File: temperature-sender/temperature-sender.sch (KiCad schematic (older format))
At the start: 33 parts, among them K1 SERVO, P1 CONN_01X02, P2 CONN_01X02, P3 CONN_01X02, P4 CONN_01X02, P5 CONN_01X02, P6 MICRO-USB-RCT, P7 CONN_01X01, P8 CONN_01X05, SW1 SW_PUSH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

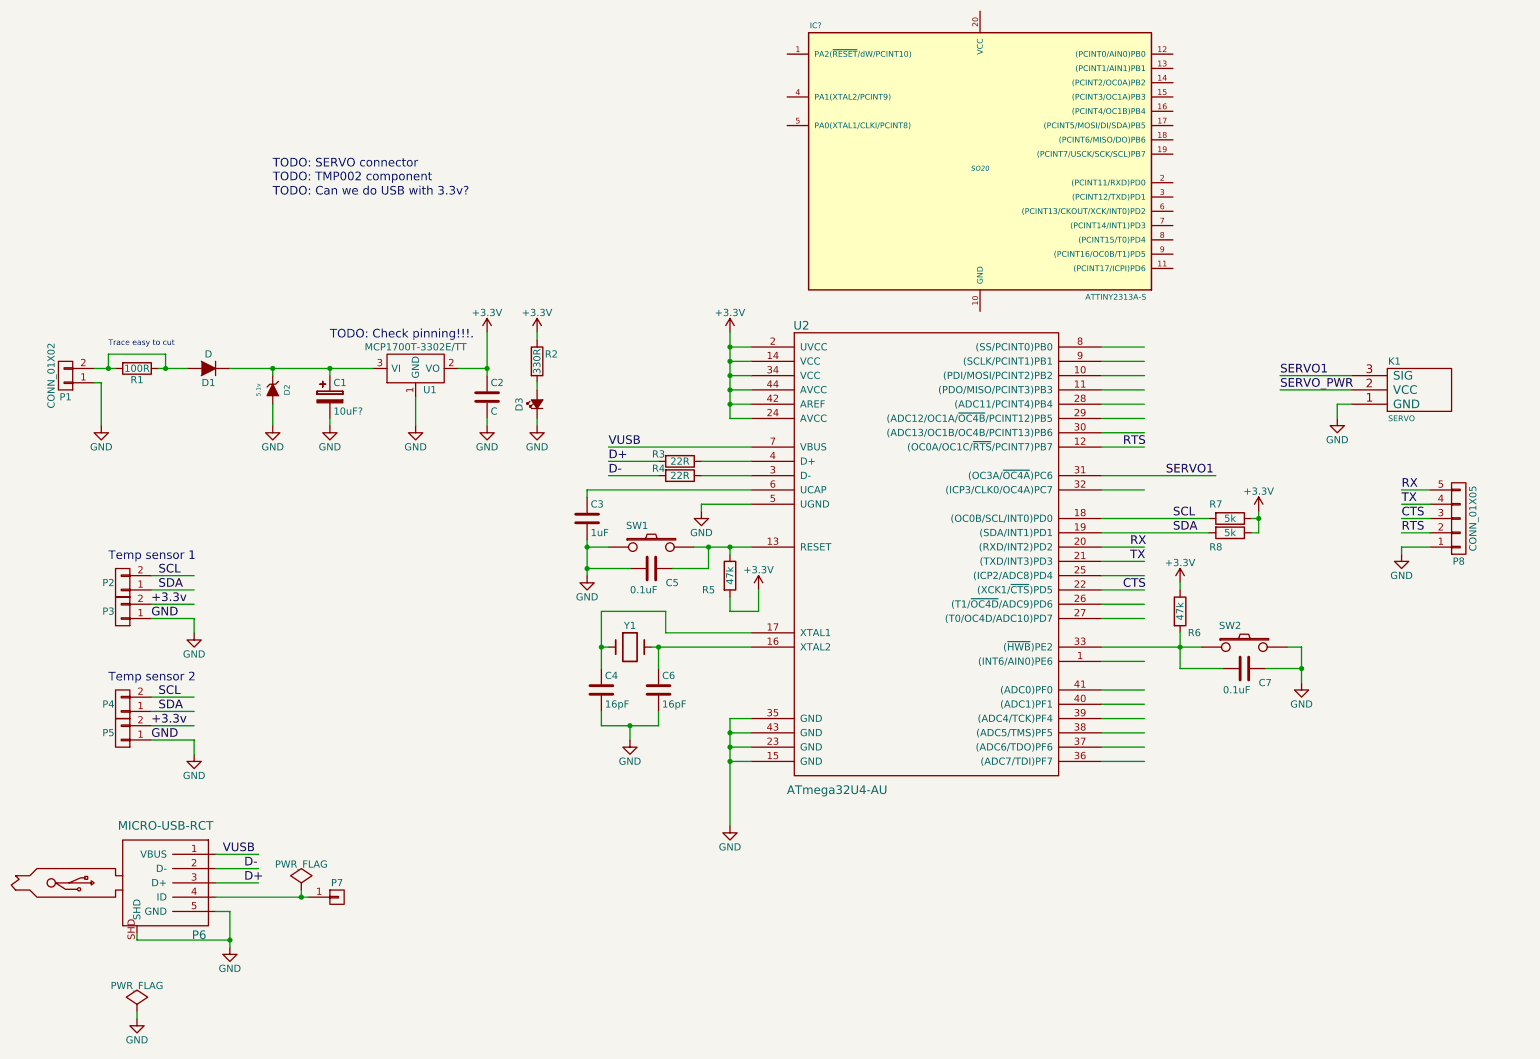
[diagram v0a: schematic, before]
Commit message: More changes to temperature-sender
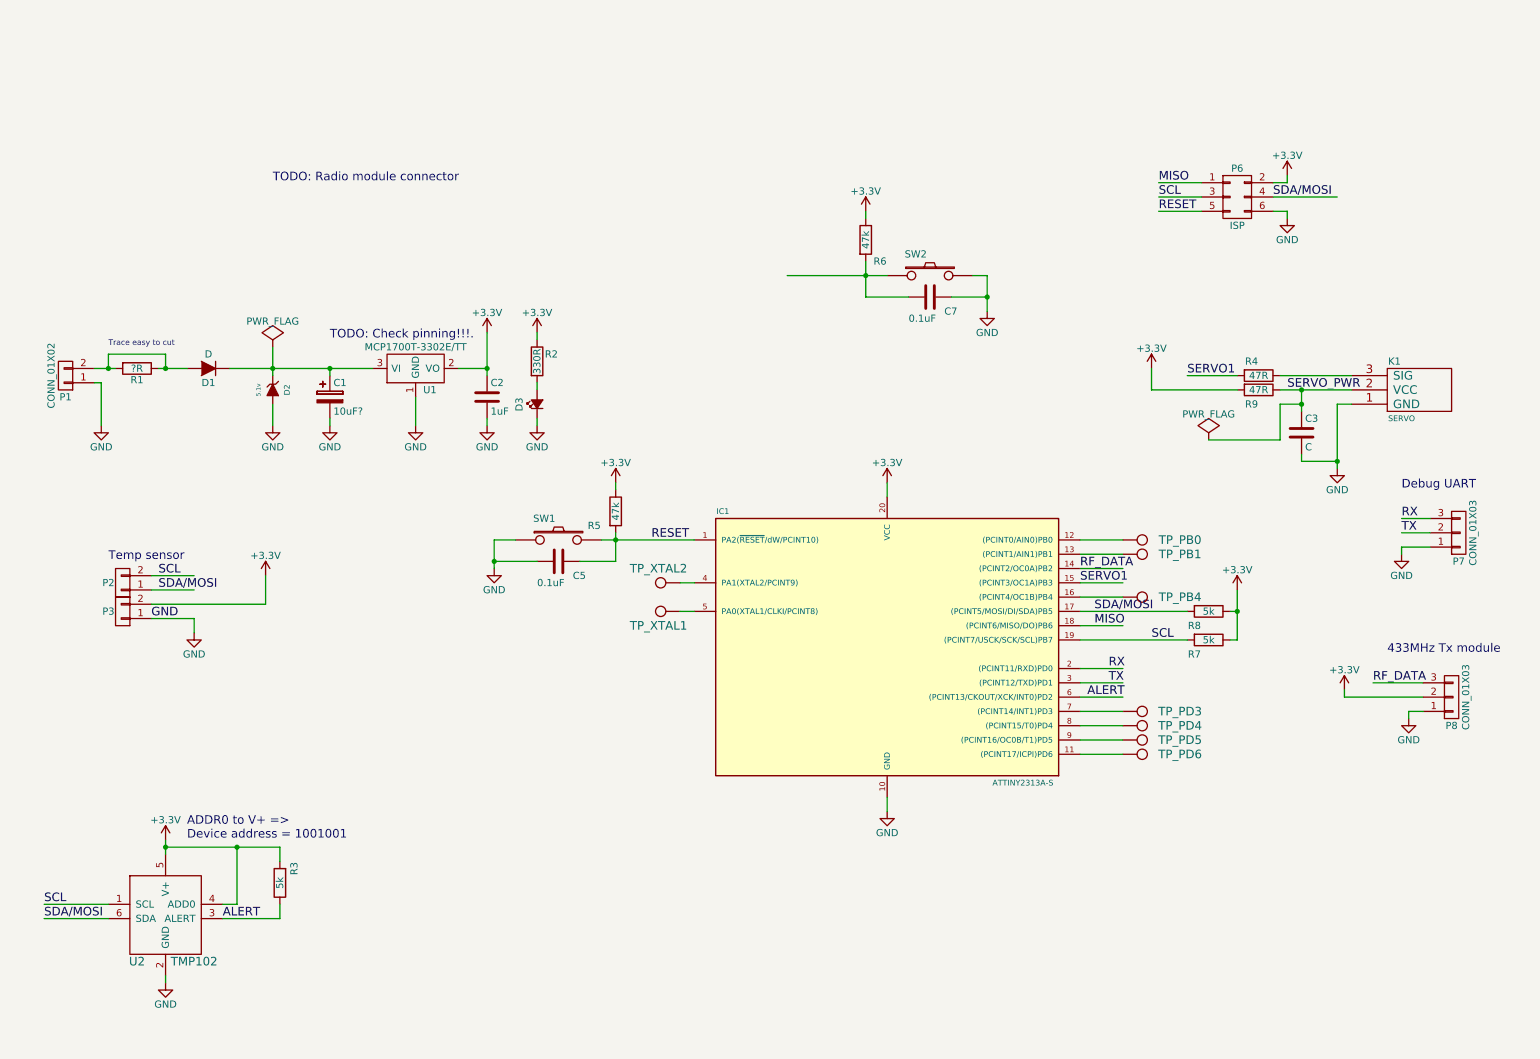
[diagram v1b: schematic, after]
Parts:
- removed C4, C6: 16pF, Capacitors_SMD:C_0603_HandSoldering, symbol C
- removed P4, P5: CONN_01X02, Pin_Headers:Pin_Header_Angled_1x02, symbol CONN_01X02
- removed P6: MICRO-USB-RCT, symbol MICRO-USB-RCT
- removed P7: CONN_01X01, symbol CONN_01X01
- removed P8: CONN_01X05, symbol CONN_01X05
- removed U2: ATmega32U4-AU, Housings_QFP:TQFP-44_10x10mm_Pitch0.8mm, symbol ATmega32U4-AU
- removed Y1: Crystal, symbol Crystal
- added P6: ISP, Socket_Strips:Socket_Strip_Straight_2x03, symbol CONN_02X03
- added P7, P8: CONN_01X03, kicad-footprints:Pin_Header_Angled_SMD_1x03, symbol CONN_01X03
- added R9: 47R, Resistors_SMD:R_0603_HandSoldering, symbol R
- added TP_PB0, TP_PB1, TP_PB4, TP_PD3, TP_PD4, TP_PD5, TP_PD6, TP_XTAL1, TP_XTAL2: TEST_POINT, kicad-footprints:TP_1mm, symbol TEST_POINT
- added U2: TMP102, kicad-footprints:SOT563, symbol TMP102
- C2: value C -> 1uF
- C3: value 1uF -> C; footprint Capacitors_SMD:C_0603_HandSoldering -> (none)
- D1: footprint (none) -> kicad-footprints:DO-214AC
- D3: footprint (none) -> LEDs:LED-0603
- IC1: renamed from IC?; footprint SO20 -> Housings_SOIC:SOIC-20_7.5x12.8mm_Pitch1.27mm
- K1: footprint (none) -> kicad-footprints:Pin_Header_Angled_SMD_1x03
- P1, P2, P3: footprint Pin_Headers:Pin_Header_Angled_1x02 -> kicad-footprints:Pin_Header_Angled_SMD_1x02
- R1: value 100R -> ?R
- R3: value 22R -> 5k
- R4: value 22R -> 47R
- U1: footprint (none) -> Housings_SOT-23_SOT-143_TSOT-6:SOT-23_Handsoldering
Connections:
- net labels added: ALERT, MISO, RESET, RF_DATA, SDA/MOSI
- net labels removed: +3.3v, CTS, D+, D-, RTS, SDA, VUSB
- wire segments 126 -> 101
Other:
- note added: "433MHz Tx module"
- note added: "ADDR0 to V+ =>\nDevice address = 1001001"
- note added: "Debug UART"
- note added: "TODO: Radio module connector"
- note added: "Temp sensor"
- note removed: "TODO: Can we do USB with 3.3v?"
- note removed: "TODO: SERVO connector\nTODO: TMP002 component"
- note removed: "Temp sensor 1"
- note removed: "Temp sensor 2"
- moved on the sheet: C5, C7, IC1, R5, R6, R7, R8, SW1, SW2
